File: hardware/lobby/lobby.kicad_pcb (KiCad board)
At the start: 4 copper layers, 85 x 56 mm, 36 parts, among them J1 THD-02-R, J2 THD-20-R, J3 Micro_SD_Card_Det, J4 Conn_01x22_Female, SW1 SW_Push, SW2 SW_SPST, U1 RT9742GGJ5, U2 M.2-keyM, U3 MYLSM00502ERPL, U4 FSUSB42MX

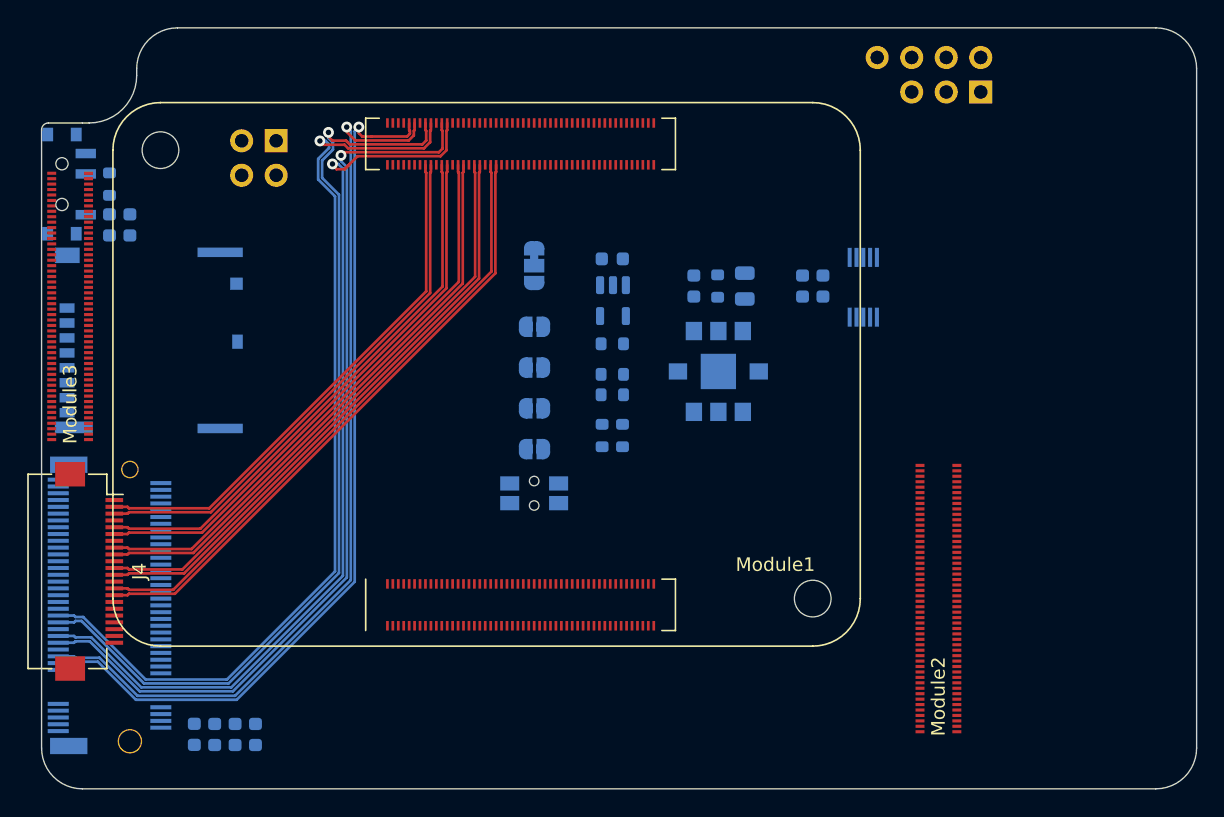
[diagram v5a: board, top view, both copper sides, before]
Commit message: finish routing on lobby
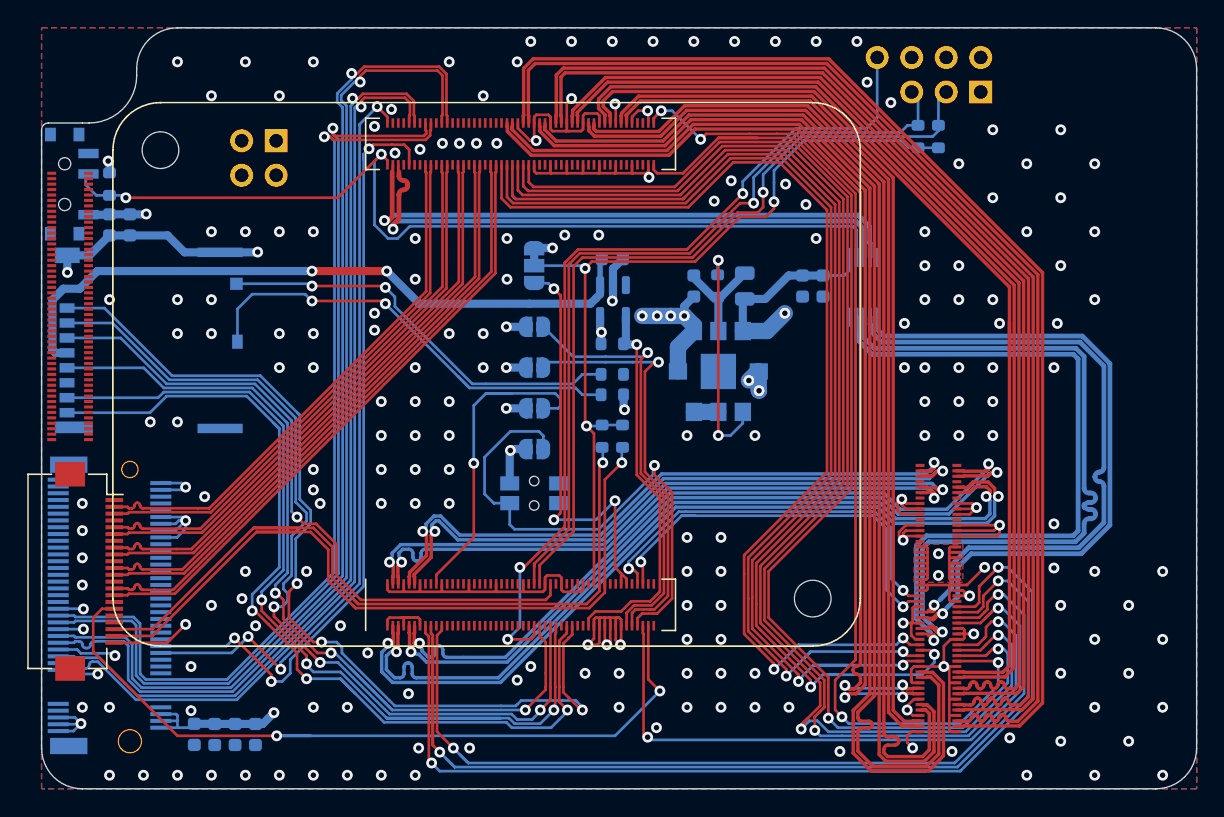
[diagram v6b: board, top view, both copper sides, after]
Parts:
- added R8: 2.2K, Resistor_SMD:R_0603_1608Metric, B.Cu at (86.0, 28.0)
- added R9: 2.2K, Resistor_SMD:R_0603_1608Metric, B.Cu at (84.5, 28.0)
- moved SW2 0.20 mm to (21.7, 31.5)
- turned R7 to -90 degrees
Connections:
- J4 pad 18: unconnected-(J4-Pad18) -> (no net)
- Module1 pad 100: unconnected-(Module1-Pad100) -> (no net)
- Module1 pad 104: unconnected-(Module1-Pad104) -> (no net)
- Module1 pad 106: unconnected-(Module1-Pad106) -> (no net)
- Module1 pad 111: unconnected-(Module1-Pad111) -> (no net)
- Module1 pad 128: unconnected-(Module1-Pad128) -> (no net)
- Module1 pad 130: unconnected-(Module1-Pad130) -> (no net)
- Module1 pad 134: unconnected-(Module1-Pad134) -> (no net)
- Module1 pad 136: unconnected-(Module1-Pad136) -> (no net)
- Module1 pad 140: unconnected-(Module1-Pad140) -> (no net)
- Module1 pad 142: unconnected-(Module1-Pad142) -> (no net)
- Module1 pad 157: unconnected-(Module1-Pad157) -> (no net)
- Module1 pad 159: unconnected-(Module1-Pad159) -> (no net)
- Module1 pad 16: unconnected-(Module1-Pad16) -> (no net)
- Module1 pad 163: unconnected-(Module1-Pad163) -> (no net)
- Module1 pad 165: unconnected-(Module1-Pad165) -> (no net)
- Module1 pad 169: unconnected-(Module1-Pad169) -> (no net)
- Module1 pad 171: unconnected-(Module1-Pad171) -> (no net)
- Module1 pad 175: unconnected-(Module1-Pad175) -> (no net)
- Module1 pad 177: unconnected-(Module1-Pad177) -> (no net)
- Module1 pad 18: unconnected-(Module1-Pad18) -> (no net)
- Module1 pad 181: unconnected-(Module1-Pad181) -> (no net)
- Module1 pad 183: unconnected-(Module1-Pad183) -> (no net)
- Module1 pad 187: unconnected-(Module1-Pad187) -> (no net)
- Module1 pad 189: unconnected-(Module1-Pad189) -> (no net)
- Module1 pad 19: unconnected-(Module1-Pad19) -> (no net)
- Module1 pad 193: unconnected-(Module1-Pad193) -> (no net)
- Module1 pad 194: unconnected-(Module1-Pad194) -> (no net)
- Module1 pad 195: unconnected-(Module1-Pad195) -> (no net)
- Module1 pad 196: unconnected-(Module1-Pad196) -> (no net)
- Module1 pad 24: /GPIO26 -> (no net)
- Module1 pad 25: /GPIO21 -> (no net)
- Module1 pad 26: /GPIO19 -> (no net)
- Module1 pad 27: /GPIO20 -> (no net)
- Module1 pad 28: /GPIO13 -> (no net)
- Module1 pad 29: /GPIO16 -> (no net)
- Module1 pad 30: /GPIO6 -> (no net)
- Module1 pad 31: /GPIO12 -> (no net)
- Module1 pad 34: /GPIO5 -> (no net)
- Module1 pad 35: /ID_SC -> (no net)
- Module1 pad 36: /ID_SD -> (no net)
- Module1 pad 37: /GPIO7 -> (no net)
- Module1 pad 38: /GPIO11 -> (no net)
- Module1 pad 39: /GPIO8 -> (no net)
- Module1 pad 40: /GPIO9 -> (no net)
- Module1 pad 41: /GPIO25 -> (no net)
- Module1 pad 44: /GPIO10 -> (no net)
- Module1 pad 45: /GPIO24 -> (no net)
- Module1 pad 46: /GPIO22 -> (no net)
- Module1 pad 47: /GPIO23 -> (no net)
- Module1 pad 48: /GPIO27 -> (no net)
- Module1 pad 49: /GPIO18 -> (no net)
- Module1 pad 50: /GPIO17 -> (no net)
- Module1 pad 51: /GPIO15 -> (no net)
- Module1 pad 54: /GPIO4 -> (no net)
- Module1 pad 64: unconnected-(Module1-Pad64) -> (no net)
- Module1 pad 68: unconnected-(Module1-Pad68) -> (no net)
- Module1 pad 70: unconnected-(Module1-Pad70) -> (no net)
- Module1 pad 72: unconnected-(Module1-Pad72) -> (no net)
- Module1 pad 73: unconnected-(Module1-Pad73) -> (no net)
- Module1 pad 76: unconnected-(Module1-Pad76) -> (no net)
- Module1 pad 84: unconnected-(Module1-Pad84) -> (no net)
- Module1 pad 86: unconnected-(Module1-Pad86) -> (no net)
- Module1 pad 88: unconnected-(Module1-Pad88) -> /+1.8v
- Module1 pad 90: unconnected-(Module1-Pad90) -> /+1.8v
- Module1 pad 92: unconnected-(Module1-Pad92) -> (no net)
- Module1 pad 99: unconnected-(Module1-Pad99) -> (no net)
- Module3 pad 1: unconnected-(Module3-Pad1) -> (no net)
- Module3 pad 10: unconnected-(Module3-Pad10) -> (no net)
- Module3 pad 100: unconnected-(Module3-Pad100) -> (no net)
- Module3 pad 11: unconnected-(Module3-Pad11) -> (no net)
- Module3 pad 12: unconnected-(Module3-Pad12) -> (no net)
- Module3 pad 13: unconnected-(Module3-Pad13) -> (no net)
- Module3 pad 14: unconnected-(Module3-Pad14) -> (no net)
- Module3 pad 15: unconnected-(Module3-Pad15) -> (no net)
- Module3 pad 16: unconnected-(Module3-Pad16) -> (no net)
- Module3 pad 17: unconnected-(Module3-Pad17) -> (no net)
- Module3 pad 18: unconnected-(Module3-Pad18) -> (no net)
- Module3 pad 19: unconnected-(Module3-Pad19) -> (no net)
- Module3 pad 2: unconnected-(Module3-Pad2) -> (no net)
- Module3 pad 20: unconnected-(Module3-Pad20) -> (no net)
- Module3 pad 21: unconnected-(Module3-Pad21) -> (no net)
- Module3 pad 22: unconnected-(Module3-Pad22) -> (no net)
- Module3 pad 23: unconnected-(Module3-Pad23) -> (no net)
- Module3 pad 24: unconnected-(Module3-Pad24) -> (no net)
- Module3 pad 25: unconnected-(Module3-Pad25) -> (no net)
- Module3 pad 26: unconnected-(Module3-Pad26) -> (no net)
- Module3 pad 27: unconnected-(Module3-Pad27) -> (no net)
- Module3 pad 28: unconnected-(Module3-Pad28) -> (no net)
- Module3 pad 29: unconnected-(Module3-Pad29) -> (no net)
- Module3 pad 3: unconnected-(Module3-Pad3) -> (no net)
- Module3 pad 30: unconnected-(Module3-Pad30) -> (no net)
- Module3 pad 31: unconnected-(Module3-Pad31) -> (no net)
- Module3 pad 32: unconnected-(Module3-Pad32) -> (no net)
- Module3 pad 33: unconnected-(Module3-Pad33) -> (no net)
- Module3 pad 34: unconnected-(Module3-Pad34) -> (no net)
- Module3 pad 35: unconnected-(Module3-Pad35) -> (no net)
- Module3 pad 36: unconnected-(Module3-Pad36) -> (no net)
- Module3 pad 37: unconnected-(Module3-Pad37) -> (no net)
- Module3 pad 38: unconnected-(Module3-Pad38) -> (no net)
- Module3 pad 39: unconnected-(Module3-Pad39) -> (no net)
- Module3 pad 4: unconnected-(Module3-Pad4) -> (no net)
- Module3 pad 40: unconnected-(Module3-Pad40) -> (no net)
- Module3 pad 41: unconnected-(Module3-Pad41) -> (no net)
- Module3 pad 42: unconnected-(Module3-Pad42) -> (no net)
- Module3 pad 43: unconnected-(Module3-Pad43) -> (no net)
- Module3 pad 44: unconnected-(Module3-Pad44) -> (no net)
- Module3 pad 45: unconnected-(Module3-Pad45) -> (no net)
- Module3 pad 46: unconnected-(Module3-Pad46) -> (no net)
- Module3 pad 47: unconnected-(Module3-Pad47) -> (no net)
- Module3 pad 48: unconnected-(Module3-Pad48) -> (no net)
- Module3 pad 49: unconnected-(Module3-Pad49) -> (no net)
- Module3 pad 5: unconnected-(Module3-Pad5) -> (no net)
- Module3 pad 50: unconnected-(Module3-Pad50) -> (no net)
- Module3 pad 51: unconnected-(Module3-Pad51) -> (no net)
- Module3 pad 52: unconnected-(Module3-Pad52) -> (no net)
- Module3 pad 53: unconnected-(Module3-Pad53) -> (no net)
- Module3 pad 54: unconnected-(Module3-Pad54) -> (no net)
- Module3 pad 55: unconnected-(Module3-Pad55) -> (no net)
- Module3 pad 56: unconnected-(Module3-Pad56) -> (no net)
- Module3 pad 57: unconnected-(Module3-Pad57) -> (no net)
- Module3 pad 58: unconnected-(Module3-Pad58) -> (no net)
- Module3 pad 59: unconnected-(Module3-Pad59) -> (no net)
- Module3 pad 6: unconnected-(Module3-Pad6) -> (no net)
- Module3 pad 60: unconnected-(Module3-Pad60) -> (no net)
- Module3 pad 61: unconnected-(Module3-Pad61) -> (no net)
- Module3 pad 62: unconnected-(Module3-Pad62) -> (no net)
- Module3 pad 63: unconnected-(Module3-Pad63) -> (no net)
- Module3 pad 64: unconnected-(Module3-Pad64) -> (no net)
- Module3 pad 65: unconnected-(Module3-Pad65) -> (no net)
- Module3 pad 66: unconnected-(Module3-Pad66) -> (no net)
- Module3 pad 67: unconnected-(Module3-Pad67) -> (no net)
- Module3 pad 68: unconnected-(Module3-Pad68) -> (no net)
- Module3 pad 69: unconnected-(Module3-Pad69) -> (no net)
- Module3 pad 7: unconnected-(Module3-Pad7) -> (no net)
- Module3 pad 70: unconnected-(Module3-Pad70) -> (no net)
- Module3 pad 71: unconnected-(Module3-Pad71) -> (no net)
- Module3 pad 72: unconnected-(Module3-Pad72) -> (no net)
- Module3 pad 73: unconnected-(Module3-Pad73) -> (no net)
- Module3 pad 74: unconnected-(Module3-Pad74) -> (no net)
- Module3 pad 75: unconnected-(Module3-Pad75) -> (no net)
- Module3 pad 76: unconnected-(Module3-Pad76) -> (no net)
- Module3 pad 77: unconnected-(Module3-Pad77) -> (no net)
- Module3 pad 78: unconnected-(Module3-Pad78) -> (no net)
- Module3 pad 79: unconnected-(Module3-Pad79) -> (no net)
- Module3 pad 8: unconnected-(Module3-Pad8) -> (no net)
- Module3 pad 80: unconnected-(Module3-Pad80) -> (no net)
- Module3 pad 81: unconnected-(Module3-Pad81) -> (no net)
- Module3 pad 82: unconnected-(Module3-Pad82) -> (no net)
- Module3 pad 83: unconnected-(Module3-Pad83) -> (no net)
- Module3 pad 84: unconnected-(Module3-Pad84) -> (no net)
- Module3 pad 85: unconnected-(Module3-Pad85) -> (no net)
- Module3 pad 86: unconnected-(Module3-Pad86) -> (no net)
- Module3 pad 87: unconnected-(Module3-Pad87) -> (no net)
- Module3 pad 88: unconnected-(Module3-Pad88) -> (no net)
- Module3 pad 89: unconnected-(Module3-Pad89) -> (no net)
- Module3 pad 9: unconnected-(Module3-Pad9) -> (no net)
- Module3 pad 90: unconnected-(Module3-Pad90) -> (no net)
- Module3 pad 91: unconnected-(Module3-Pad91) -> (no net)
- Module3 pad 92: unconnected-(Module3-Pad92) -> (no net)
- Module3 pad 93: unconnected-(Module3-Pad93) -> (no net)
- Module3 pad 94: unconnected-(Module3-Pad94) -> (no net)
- Module3 pad 95: unconnected-(Module3-Pad95) -> (no net)
- Module3 pad 96: unconnected-(Module3-Pad96) -> (no net)
- Module3 pad 97: unconnected-(Module3-Pad97) -> (no net)
- Module3 pad 98: unconnected-(Module3-Pad98) -> (no net)
- Module3 pad 99: unconnected-(Module3-Pad99) -> (no net)
- R4 pad 1: /sd/Reserved -> (no net)
- U1 pad 3: unconnected-(U1-Pad3) -> (no net)
- U2 pad 10: unconnected-(U2-Pad10) -> (no net)
- U2 pad 11: unconnected-(U2-Pad11) -> (no net)
- U2 pad 13: unconnected-(U2-Pad13) -> (no net)
- U2 pad 17: unconnected-(U2-Pad17) -> (no net)
- U2 pad 19: unconnected-(U2-Pad19) -> (no net)
- U2 pad 20: unconnected-(U2-Pad20) -> (no net)
- U2 pad 22: unconnected-(U2-Pad22) -> (no net)
- U2 pad 23: unconnected-(U2-Pad23) -> (no net)
- U2 pad 24: unconnected-(U2-Pad24) -> (no net)
- U2 pad 25: unconnected-(U2-Pad25) -> (no net)
- U2 pad 26: unconnected-(U2-Pad26) -> (no net)
- U2 pad 28: unconnected-(U2-Pad28) -> (no net)
- U2 pad 29: unconnected-(U2-Pad29) -> (no net)
- U2 pad 30: unconnected-(U2-Pad30) -> (no net)
- U2 pad 31: unconnected-(U2-Pad31) -> (no net)
- U2 pad 32: unconnected-(U2-Pad32) -> (no net)
- U2 pad 34: unconnected-(U2-Pad34) -> (no net)
- U2 pad 35: unconnected-(U2-Pad35) -> (no net)
- U2 pad 36: unconnected-(U2-Pad36) -> (no net)
- U2 pad 37: unconnected-(U2-Pad37) -> (no net)
- U2 pad 38: unconnected-(U2-Pad38) -> (no net)
- U2 pad 40: unconnected-(U2-Pad40) -> (no net)
- U2 pad 42: unconnected-(U2-Pad42) -> (no net)
- U2 pad 44: unconnected-(U2-Pad44) -> (no net)
- U2 pad 46: unconnected-(U2-Pad46) -> (no net)
- U2 pad 48: unconnected-(U2-Pad48) -> (no net)
- U2 pad 5: unconnected-(U2-Pad5) -> (no net)
- U2 pad 54: unconnected-(U2-Pad54) -> (no net)
- U2 pad 56: unconnected-(U2-Pad56) -> (no net)
- U2 pad 58: unconnected-(U2-Pad58) -> (no net)
- U2 pad 6: unconnected-(U2-Pad6) -> (no net)
- U2 pad 67: unconnected-(U2-Pad67) -> (no net)
- U2 pad 68: unconnected-(U2-Pad68) -> (no net)
- U2 pad 69: unconnected-(U2-Pad69) -> (no net)
- U2 pad 7: unconnected-(U2-Pad7) -> (no net)
- U2 pad 8: unconnected-(U2-Pad8) -> (no net)
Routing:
- net /+3.3v: track 0.00 -> 240.5 mm, vias 0 -> 10
- net /+5v: track 0.00 -> 167.8 mm, vias 0 -> 11
- net GND: track 0.00 -> 148.5 mm, vias 0 -> 203
- net /HDMI0_HOTPLUG: track 0.00 -> 98.8 mm, vias 0 -> 2
- net /HDMI0_CEC: track 0.00 -> 98.2 mm, vias 0 -> 2
- net /HDMI1_TX1_P: track 0.00 -> 87.7 mm
- net /HDMI1_TX1_N: track 0.00 -> 87.6 mm
- net /HDMI1_TX0_P: track 0.00 -> 85.4 mm
- net /HDMI1_TX0_N: track 0.00 -> 85.3 mm
- net /HDMI0_SDA: track 0.00 -> 85.0 mm, vias 0 -> 2
- net /HDMI1_CLK_P: track 0.00 -> 82.2 mm
- net /HDMI1_CLK_N: track 0.00 -> 82.1 mm
- net /HDMI1_CEC: track 0.00 -> 81.2 mm, vias 0 -> 2
- net /HDMI1_SCL: track 0.00 -> 80.5 mm, vias 0 -> 2
- net /TR3_TAP: track 0.00 -> 79.5 mm, vias 0 -> 1
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- added copper zone on F.Cu, net /+5v
- added copper zone on B.Cu, net GND
- added copper zone on F.Cu, net GND
- added copper zone on In1.Cu, net GND
- added copper zone on In2.Cu, net GND

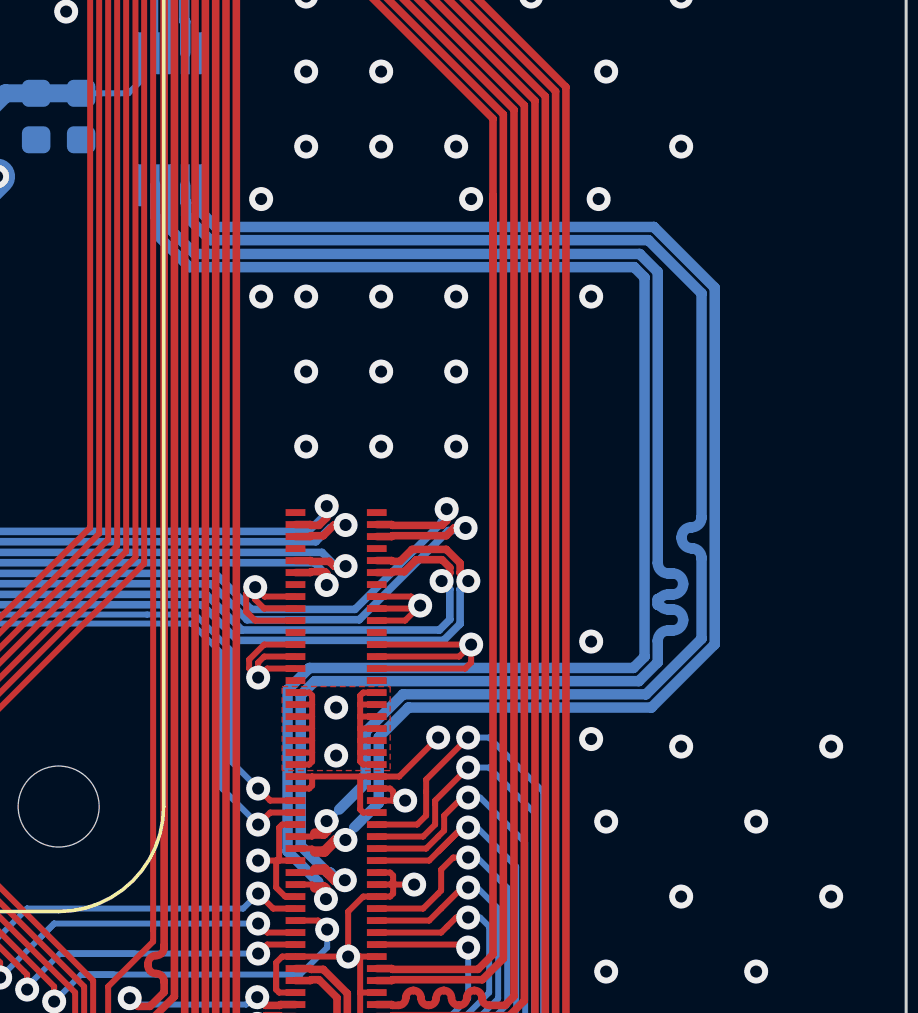
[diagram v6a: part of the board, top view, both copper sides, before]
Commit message: adjust USB dp tune
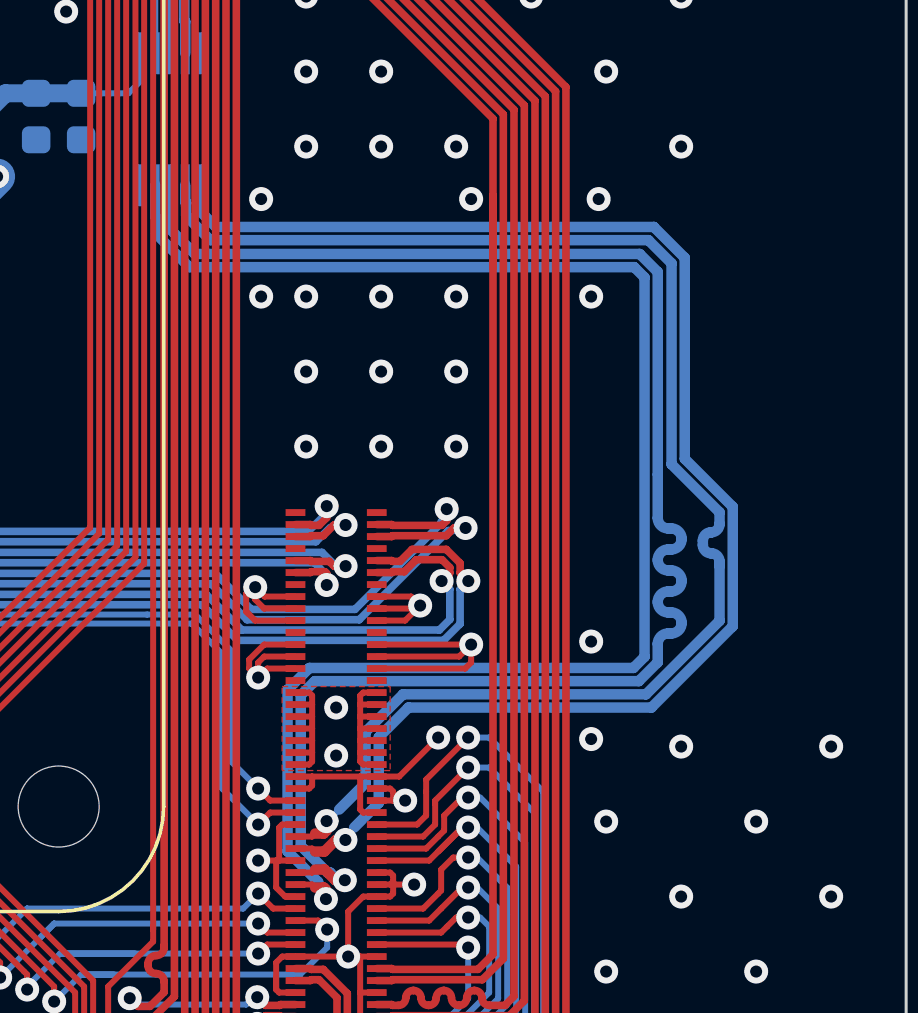
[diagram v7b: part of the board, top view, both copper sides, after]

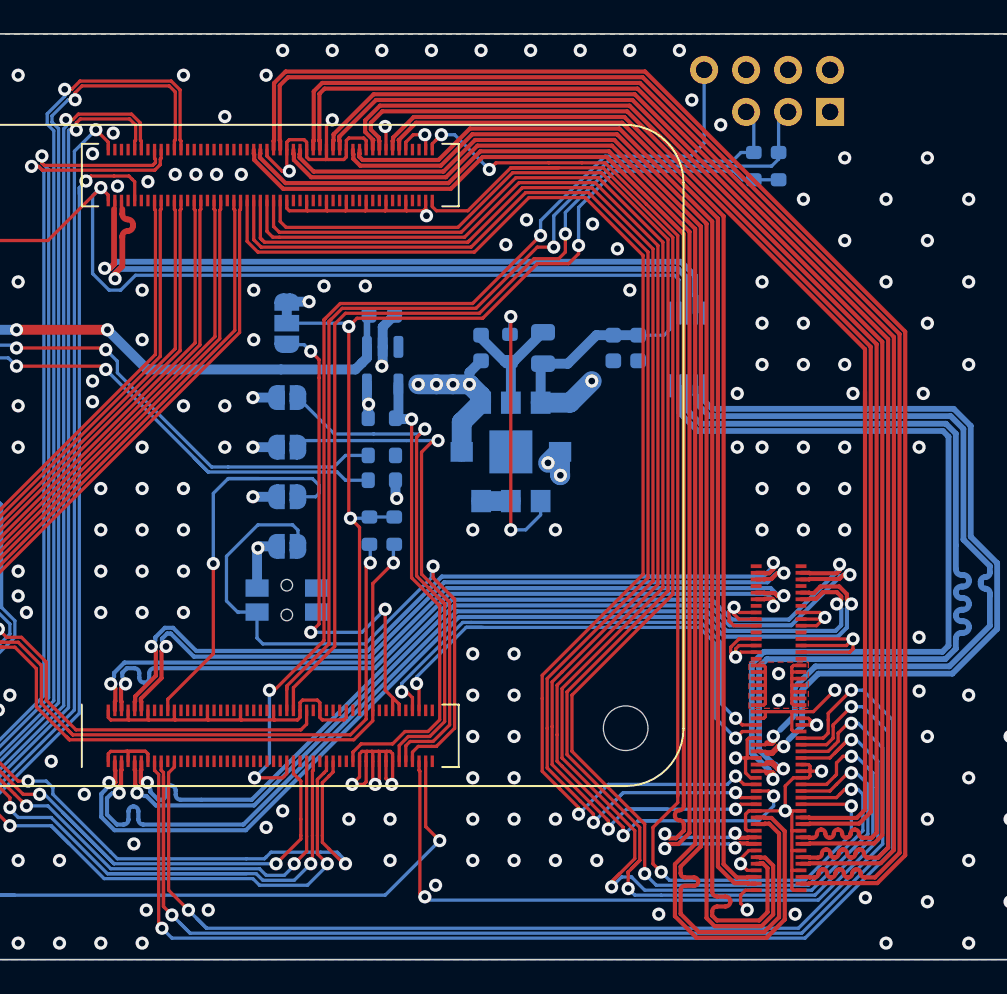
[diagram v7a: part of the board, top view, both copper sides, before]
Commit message: tweak lobby
pushed traces for wifi clearance zone
improved cm4 footprint
improved usb-c footprint
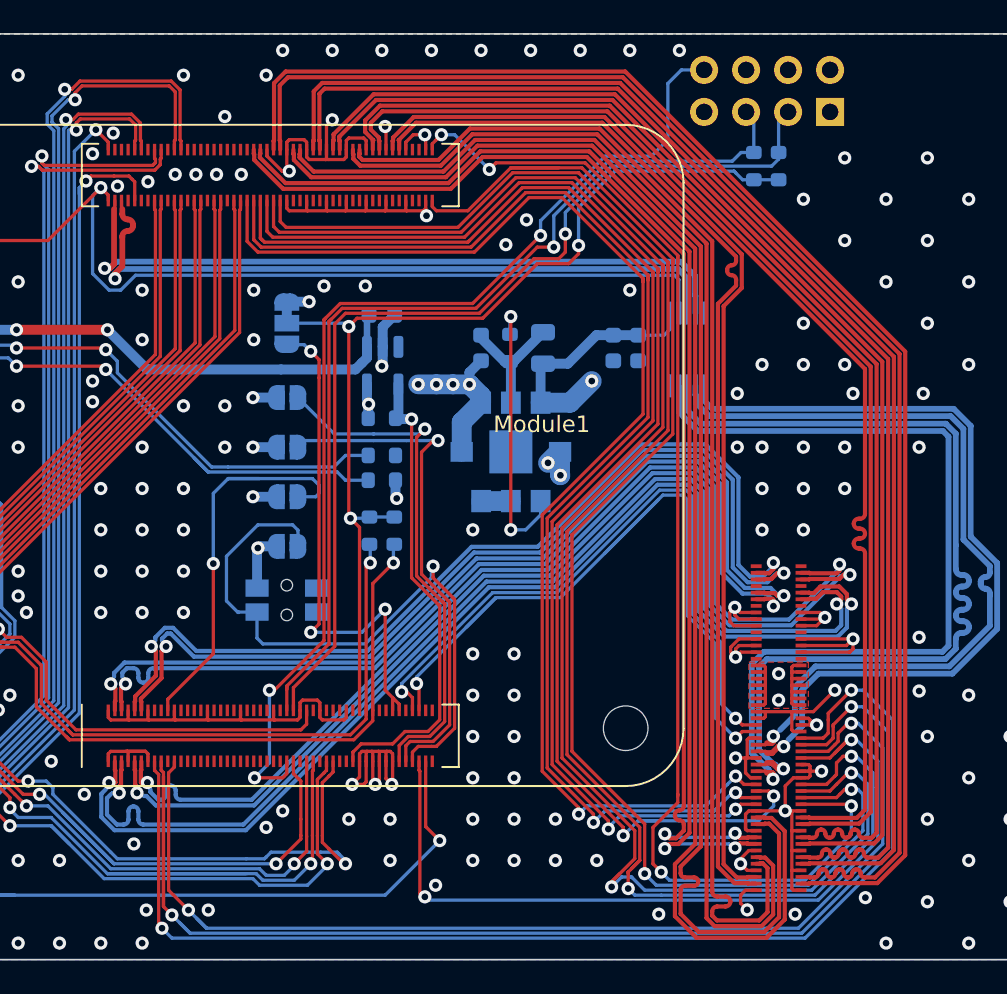
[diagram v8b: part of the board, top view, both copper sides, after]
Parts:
- Module1: footprint cm4crypto:Raspberry-Pi-4-Compute-Module -> cm4crypto:Raspberry-Pi-4-Compute-Module-diagonal-mount-bl-ur
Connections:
- Module1 pad 100: (no net) -> unconnected-(Module1-Pad100)
- Module1 pad 104: (no net) -> unconnected-(Module1-Pad104)
- Module1 pad 106: (no net) -> unconnected-(Module1-Pad106)
- Module1 pad 111: (no net) -> unconnected-(Module1-Pad111)
- Module1 pad 128: (no net) -> unconnected-(Module1-Pad128)
- Module1 pad 130: (no net) -> unconnected-(Module1-Pad130)
- Module1 pad 134: (no net) -> unconnected-(Module1-Pad134)
- Module1 pad 136: (no net) -> unconnected-(Module1-Pad136)
- Module1 pad 140: (no net) -> unconnected-(Module1-Pad140)
- Module1 pad 142: (no net) -> unconnected-(Module1-Pad142)
- Module1 pad 157: (no net) -> unconnected-(Module1-Pad157)
- Module1 pad 159: (no net) -> unconnected-(Module1-Pad159)
- Module1 pad 16: (no net) -> unconnected-(Module1-Pad16)
- Module1 pad 163: (no net) -> unconnected-(Module1-Pad163)
- Module1 pad 165: (no net) -> unconnected-(Module1-Pad165)
- Module1 pad 169: (no net) -> unconnected-(Module1-Pad169)
- Module1 pad 171: (no net) -> unconnected-(Module1-Pad171)
- Module1 pad 175: (no net) -> unconnected-(Module1-Pad175)
- Module1 pad 177: (no net) -> unconnected-(Module1-Pad177)
- Module1 pad 18: (no net) -> unconnected-(Module1-Pad18)
- Module1 pad 181: (no net) -> unconnected-(Module1-Pad181)
- Module1 pad 183: (no net) -> unconnected-(Module1-Pad183)
- Module1 pad 187: (no net) -> unconnected-(Module1-Pad187)
- Module1 pad 189: (no net) -> unconnected-(Module1-Pad189)
- Module1 pad 19: (no net) -> unconnected-(Module1-Pad19)
- Module1 pad 193: (no net) -> unconnected-(Module1-Pad193)
- Module1 pad 194: (no net) -> unconnected-(Module1-Pad194)
- Module1 pad 195: (no net) -> unconnected-(Module1-Pad195)
- Module1 pad 196: (no net) -> unconnected-(Module1-Pad196)
- Module1 pad 24: (no net) -> /GPIO26
- Module1 pad 25: (no net) -> /GPIO21
- Module1 pad 26: (no net) -> /GPIO19
- Module1 pad 27: (no net) -> /GPIO20
- Module1 pad 28: (no net) -> /GPIO13
- Module1 pad 29: (no net) -> /GPIO16
- Module1 pad 30: (no net) -> /GPIO6
- Module1 pad 31: (no net) -> /GPIO12
- Module1 pad 34: (no net) -> /GPIO5
- Module1 pad 35: (no net) -> /ID_SC
- Module1 pad 36: (no net) -> /ID_SD
- Module1 pad 37: (no net) -> /GPIO7
- Module1 pad 38: (no net) -> /GPIO11
- Module1 pad 39: (no net) -> /GPIO8
- Module1 pad 40: (no net) -> /GPIO9
- Module1 pad 41: (no net) -> /GPIO25
- Module1 pad 44: (no net) -> /GPIO10
- Module1 pad 45: (no net) -> /GPIO24
- Module1 pad 46: (no net) -> /GPIO22
- Module1 pad 47: (no net) -> /GPIO23
- Module1 pad 48: (no net) -> /GPIO27
- Module1 pad 49: (no net) -> /GPIO18
- Module1 pad 50: (no net) -> /GPIO17
- Module1 pad 51: (no net) -> /GPIO15
- Module1 pad 54: (no net) -> /GPIO4
- Module1 pad 64: (no net) -> unconnected-(Module1-Pad64)
- Module1 pad 68: (no net) -> unconnected-(Module1-Pad68)
- Module1 pad 70: (no net) -> unconnected-(Module1-Pad70)
- Module1 pad 72: (no net) -> unconnected-(Module1-Pad72)
- Module1 pad 73: (no net) -> unconnected-(Module1-Pad73)
- Module1 pad 76: (no net) -> unconnected-(Module1-Pad76)
- Module1 pad 84: (no net) -> unconnected-(Module1-Pad84)
- Module1 pad 86: (no net) -> unconnected-(Module1-Pad86)
- Module1 pad 92: (no net) -> unconnected-(Module1-Pad92)
- Module1 pad 99: (no net) -> unconnected-(Module1-Pad99)
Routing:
- net /AnalogIP0: track 30.7 -> 47.5 mm
- net /AnalogIP1: track 29.8 -> 45.3 mm
- net /TRD3_P: track 60.9 -> 71.6 mm
- net /TRD3_N: track 60.8 -> 71.5 mm
- net /TRD2_P: track 55.2 -> 65.9 mm
- net /TRD2_N: track 55.3 -> 66.0 mm
- net /TRD1_N: track 47.0 -> 56.7 mm
- net /TRD1_P: track 47.0 -> 56.8 mm
- net /TRD0_P: track 47.3 -> 57.1 mm
- net /TRD0_N: track 47.3 -> 57.0 mm
- net /HDMI1_SCL: track 80.5 -> 77.4 mm
- net /HDMI0_TX0_N: track 72.3 -> 70.8 mm
- net /HDMI1_SDA: track 78.9 -> 77.6 mm
- net /HDMI0_CLK_N: track 64.7 -> 65.5 mm
- net /HDMI1_TX1_P: track 87.7 -> 87.0 mm
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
